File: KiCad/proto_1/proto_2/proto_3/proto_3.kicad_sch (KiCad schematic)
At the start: 11 parts

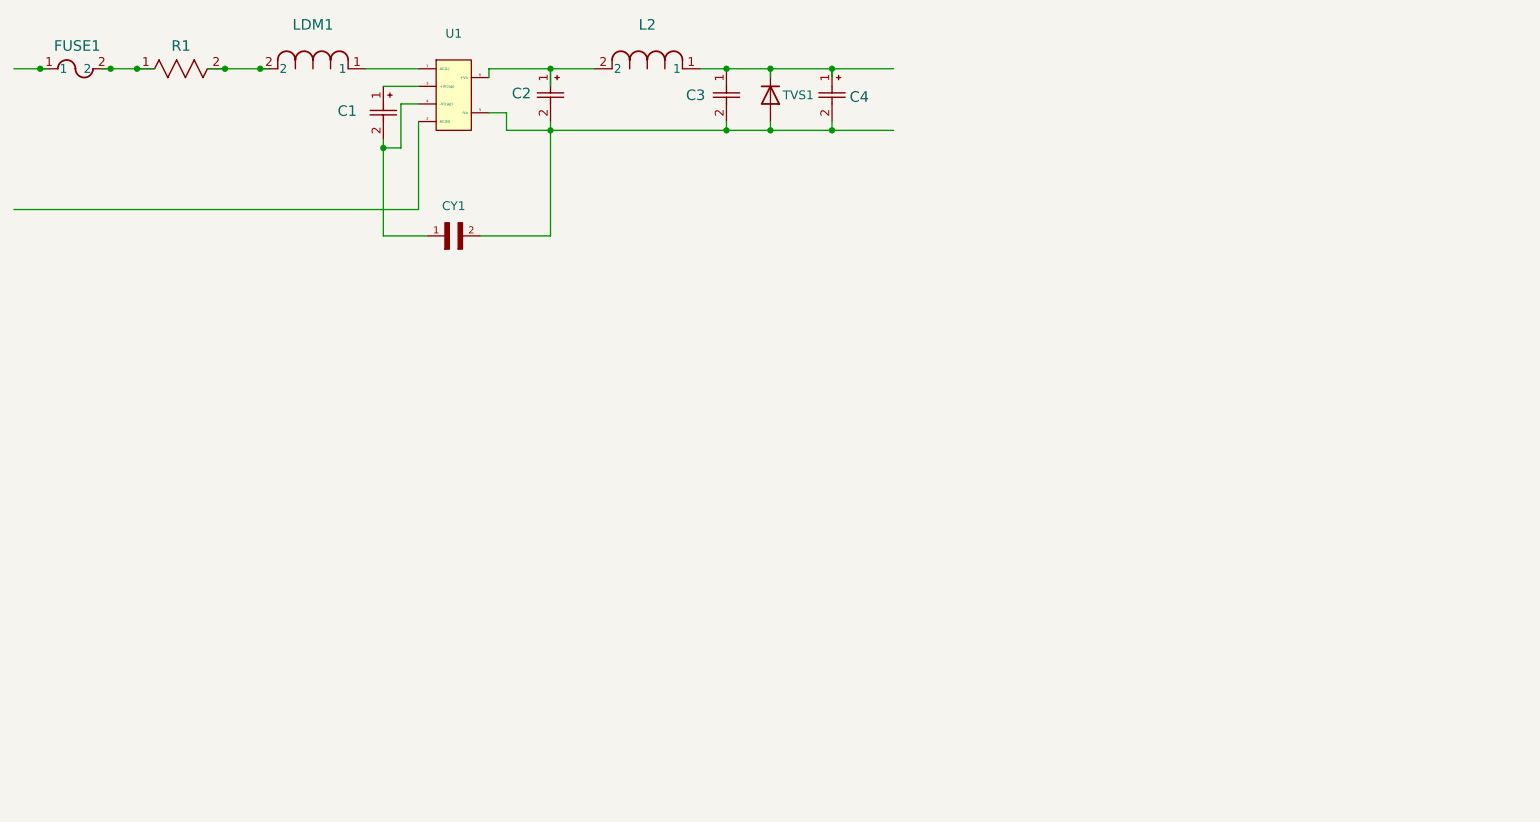
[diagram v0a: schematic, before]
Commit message: added 3d components to footprints
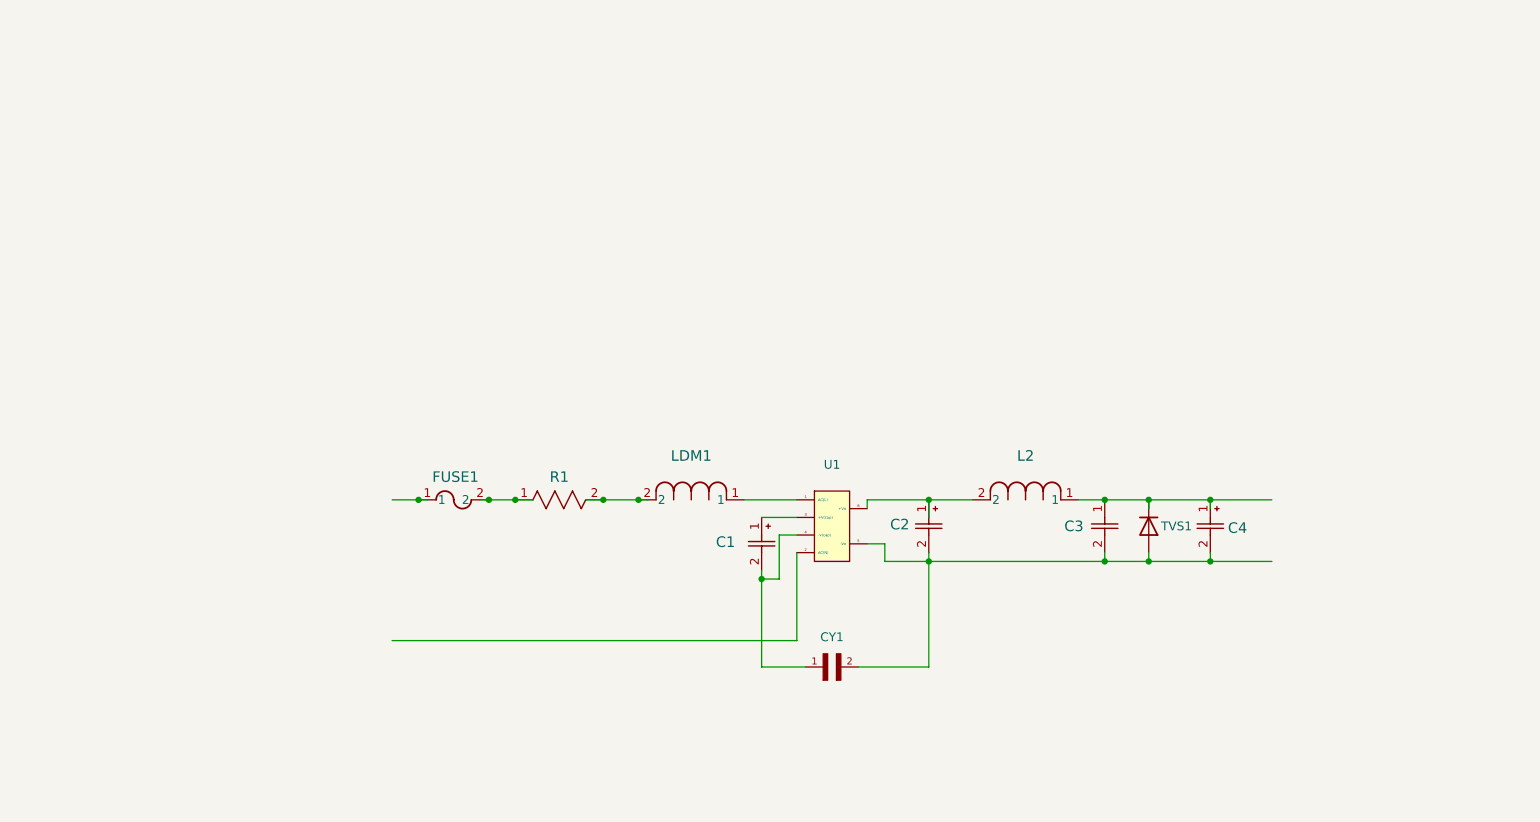
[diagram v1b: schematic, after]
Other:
- moved on the sheet: C1, C2, C3, C4, CY1, FUSE1, L2, LDM1, R1, TVS1, U1

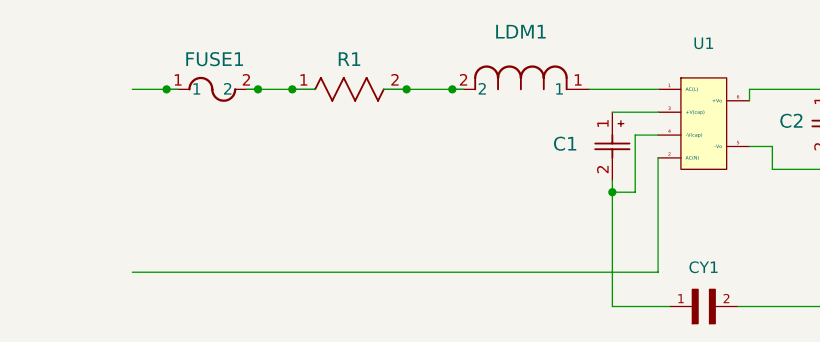
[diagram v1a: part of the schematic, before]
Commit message: Added through-holes for 120v source, moved components around on pcb
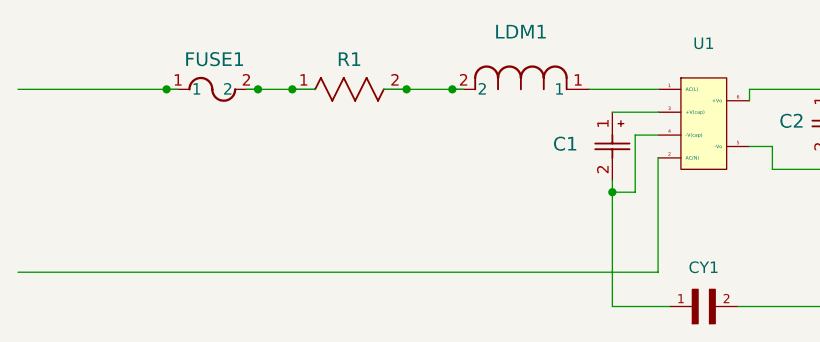
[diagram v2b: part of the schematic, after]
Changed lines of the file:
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@@
-	(wire
-		(pts
-			(xy 77.47 102.87) (xy 81.28 102.87)
-		)
-		(stroke
-			(width 0)
-			(type default)
-		)
-	)
 	(wire
 		(pts
@@
 		(pts
 			(xy 130.81 105.41) (xy 135.89 105.41)
-		)
-		(stroke
-			(width 0)
-			(type default)
-		)
-	)
-	(wire
-		(pts
-			(xy 77.47 123.19) (xy 135.89 123.19)
 		)
 		(stroke
@@
 		(pts
 			(xy 180.34 102.87) (xy 186.69 102.87)
+		)
+		(stroke
+			(width 0)
+			(type default)
+		)
+	)
+	(wire
+		(pts
+			(xy 64.77 102.87) (xy 81.28 102.87)
 		)
 		(stroke
@@
 		)
 		(stroke
+			(width 0)
+			(type default)
+		)
+	)
+	(wire
+		(pts
+			(xy 64.77 123.19) (xy 135.89 123.19)
+		)
+		(stroke

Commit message: Changed transformer footprint, moved components on pcb
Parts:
- U1: footprint stuff:power -> stuff:transformer_MPL-05SC-F
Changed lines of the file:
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@@
 			)
 		)
-		(property "Footprint" "stuff:power"
+		(property "Footprint" "stuff:transformer_MPL-05SC-F"
 			(at 141.224 111.506 0)
 			(effects

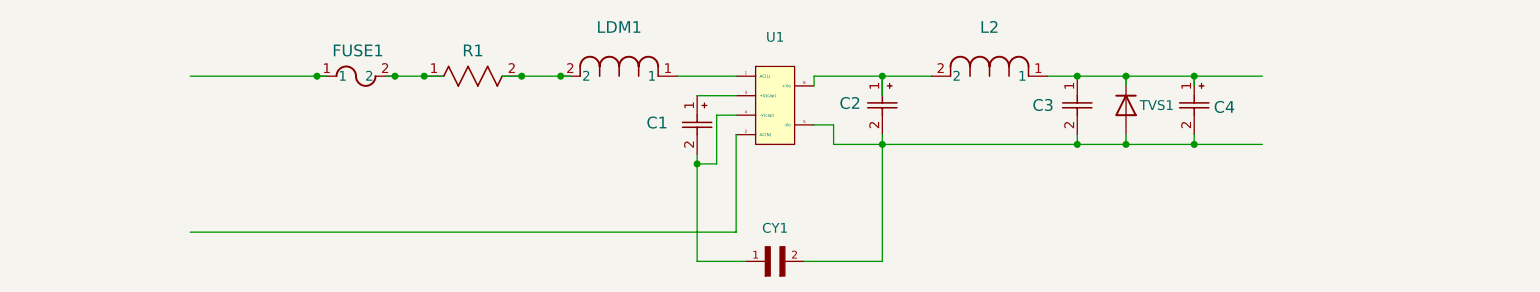
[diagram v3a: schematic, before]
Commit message: removed zips, added screw terminals, updated pcb layout
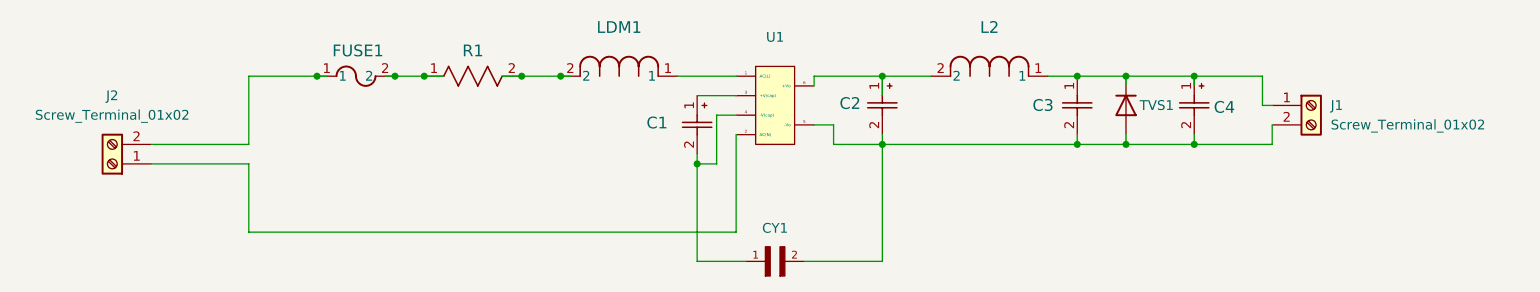
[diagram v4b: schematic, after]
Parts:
- added J1, J2: Screw_Terminal_01x02, symbol Connector:Screw_Terminal_01x02
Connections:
- net at C3.1, C4.1, L2.1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: now also J1.1 (Pin_1)
- net at C2.2, C3.2, C4.2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: now also J1.2 (Pin_2)
- net at U1.2 (AC(N)): now also J2.1 (Pin_1)
- net at FUSE1.1: now also J2.2 (Pin_2)
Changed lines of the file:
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@@
+	(wire
+		(pts
+			(xy 72.39 102.87) (xy 72.39 111.76)
+		)
+		(stroke
+			(width 0)
+			(type default)
+		)
+	)
 	(wire
 		(pts
@@
 	(wire
 		(pts
-			(xy 195.58 111.76) (xy 204.47 111.76)
+			(xy 195.58 111.76) (xy 205.74 111.76)
 		)
 		(stroke
@@
 	(wire
 		(pts
+			(xy 72.39 123.19) (xy 72.39 114.3)
+		)
+		(stroke
+			(width 0)
+			(type default)
+		)
+	)
+	(wire
+		(pts
 			(xy 130.81 105.41) (xy 135.89 105.41)
 		)
@@
 	(wire
 		(pts
+			(xy 204.47 106.68) (xy 205.74 106.68)
+		)
+		(stroke
+			(width 0)
+			(type default)
+		)
+	)
+	(wire
+		(pts
 			(xy 154.94 111.76) (xy 154.94 127)
 		)
@@
 	(wire
 		(pts
+			(xy 72.39 114.3) (xy 59.69 114.3)
+		)
+		(stroke
+			(width 0)
+			(type default)
+		)
+	)
+	(wire
+		(pts
 			(xy 180.34 102.87) (xy 186.69 102.87)
 		)
@@
 	(wire
 		(pts
-			(xy 64.77 102.87) (xy 81.28 102.87)
+			(xy 72.39 102.87) (xy 81.28 102.87)
 		)
 		(stroke
@@
 	(wire
 		(pts
+			(xy 72.39 123.19) (xy 135.89 123.19)
+		)
+		(stroke
+			(width 0)
+			(type default)
+		)
+	)
+	(wire
+		(pts
 			(xy 180.34 111.76) (xy 186.69 111.76)
 		)
@@
 	(wire
 		(pts
-			(xy 64.77 123.19) (xy 135.89 123.19)
-		)
-		(stroke
-			(width 0)
-			(type default)
-		)
-	)
-	(wire
-		(pts
 			(xy 91.44 102.87) (xy 90.17 102.87)
 		)
@@
 	(wire
 		(pts
+			(xy 59.69 111.76) (xy 72.39 111.76)
+		)
+		(stroke
+			(width 0)
+			(type default)
+		)
+	)
+	(wire
+		(pts
 			(xy 146.05 102.87) (xy 146.05 104.14)
 		)
@@
 	(wire
 		(pts
+			(xy 205.74 109.22) (xy 205.74 111.76)
+		)
+		(stroke
+			(width 0)
+			(type default)
+		)
+	)
+	(wire
+		(pts
 			(xy 97.79 102.87) (xy 95.25 102.87)
 		)
@@
 		(pts
 			(xy 195.58 110.49) (xy 195.58 111.76)
+		)
+		(stroke
+			(width 0)
+			(type default)
+		)
+	)
+	(wire
+		(pts
+			(xy 204.47 102.87) (xy 204.47 106.68)
 		)
 		(stroke
@@
 	)
 	(symbol
+		(lib_id "Connector:Screw_Terminal_01x02")
+		(at 54.61 114.3 180)
+		(unit 1)
+		(exclude_from_sim no)
+		(in_bom yes)
+		(on_board yes)
+		(dnp no)
+		(fields_autoplaced yes)
+		(property "Reference" "J2"
+			(at 54.61 105.41 0)
+			(effects
+				(font
+					(size 1.27 1.27)
+				)
+			)
+		)
+		(property "Value" "Screw_Terminal_01x02"
+			(at 54.61 107.95 0)
+			(effects
+				(font
+					(size 1.27 1.27)
+				)
+			)
+		)
+		(property "Footprint" ""
+			(at 54.61 114.3 0)
+			(effects
+				(font
+					(size 1.27 1.27)
+				)
+				(hide yes)
+			)
+		)
+		(property "Datasheet" "~"
+			(at 54.61 114.3 0)
+			(effects
+				(font
+					(size 1.27 1.27)
+				)
+				(hide yes)
+			)
+		)
+		(property "Description" "Generic screw terminal, single row, 01x02, script generated (kicad-library-utils/schlib/autogen/connector/)"
+			(at 54.61 114.3 0)
+			(effects
+				(font
+					(size 1.27 1.27)
+				)
+				(hide yes)
+			)
+		)
+		(pin "2"
+		)
+		(pin "1"
+		)
+		(instances
+			(project ""
+				(path "/3ba3c426-0aff-4728-abf4-4c9cd318aec8"
+					(reference "J2")
+					(unit 1)
+				)
+			)
+		)
+	)
+	(symbol
 		(lib_id "Capacitor-1nf-400V:DE2E3SA102MN3AY02F")
 		(at 139.7 127 0)
@@
 					(unit 1)
 				)
+			)
+		)
+	)
+	(symbol
+		(lib_id "Connector:Screw_Terminal_01x02")
+		(at 210.82 106.68 0)
+		(unit 1)
+		(exclude_from_sim no)
+		(in_bom yes)
+		(on_board yes)
+		(dnp no)
+		(fields_autoplaced yes)
+		(property "Reference" "J1"
+			(at 213.36 106.6799 0)
+			(effects
+				(font
+					(size 1.27 1.27)
+				)
+				(justify left)
+			)
+		)
+		(property "Value" "Screw_Terminal_01x02"
+			(at 213.36 109.2199 0)
+			(effects
+				(font
+					(size 1.27 1.27)
+				)
+				(justify left)
+			)
+		)
+		(property "Footprint" ""
+			(at 210.82 106.68 0)
+			(effects
+				(font
+					(size 1.27 1.27)
+				)
+				(hide yes)
+			)
+		)
+		(property "Datasheet" "~"
+			(at 210.82 106.68 0)
+			(effects
+				(font
+					(size 1.27 1.27)
+				)
+				(hide yes)
+			)
+		)
+		(property "Description" "Generic screw terminal, single row, 01x02, script generated (kicad-library-utils/schlib/autogen/connector/)"
+			(at 210.82 106.68 0)
+			(effects
+				(font
+					(size 1.27 1.27)
+				)
+				(hide yes)
+			)
+		)
+		(pin "1"
+		)
+		(pin "2"
+		)
+		(instances
+			(project ""
+				(path "/3ba3c426-0aff-4728-abf4-4c9cd318aec8"
+					(reference "J1")
+					(unit 1)
+				)

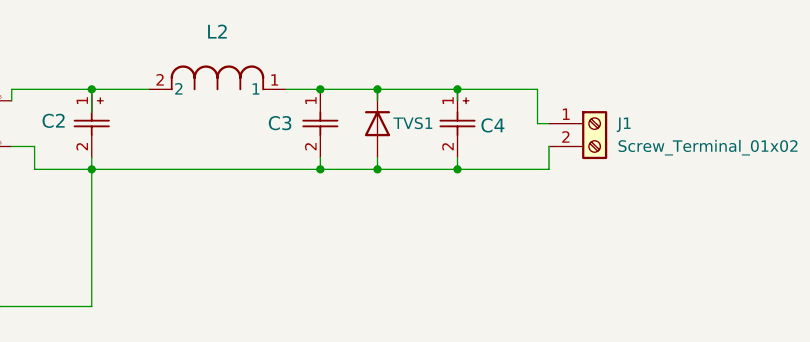
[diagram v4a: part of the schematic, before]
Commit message: added correct tvs diode
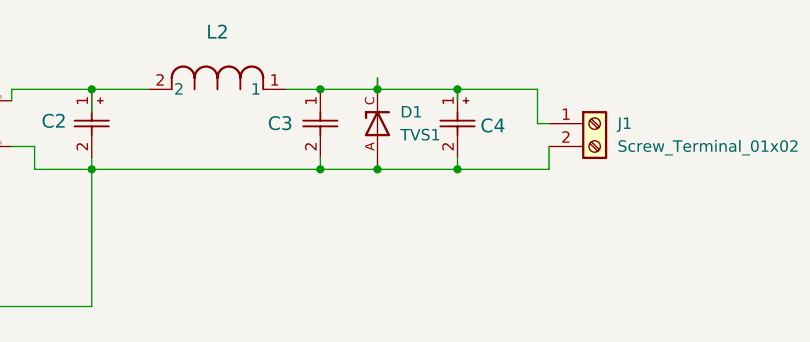
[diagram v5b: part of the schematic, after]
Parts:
- removed TVS1: ~, Diode_SMD:D_MELF, symbol Diode:SM4003
- added D1: TVS1, stuff:TVS_DIODE_9A, symbol TVS_CAP_sym:1.5KE6.8A
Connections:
- net at C3.1, C4.1, J1.1 (Pin_1)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: now also D1.C
- net at C2.2, C3.2, C4.2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: now also D1.A

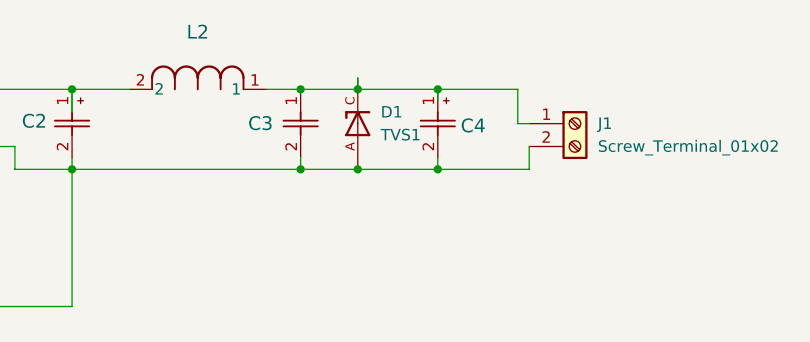
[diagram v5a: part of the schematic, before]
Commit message: removed 9A diode added 7A
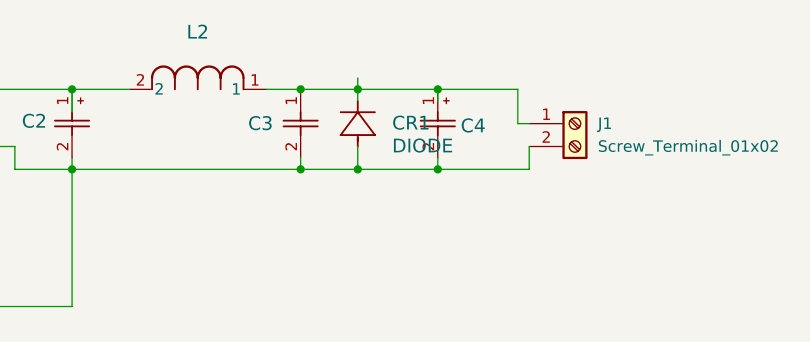
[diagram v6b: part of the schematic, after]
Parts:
- removed D1: TVS1, stuff:TVS_DIODE_9A, symbol TVS_CAP_sym:1.5KE6.8A
- added CR1: DIODE, SMBJSeries_LTF, symbol SMBJ-7A:DIODE
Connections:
- net at C2.2, C3.2, C4.2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: now also CR1.1, CR1.2
